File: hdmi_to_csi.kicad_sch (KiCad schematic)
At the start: 45 parts, among them P1 22P_FPC, U7 TC358743XBG_EL_NOK, U8 TLV62568DBVR, U9 TLV62568DBVR, X2 27MHz

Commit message: Preliminary Revision of PS176 DP->HDMI Subsystem
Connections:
- net CSI_2N: now also U7.B7 (CSID2N)
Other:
- note removed: "Solder this by hand to save money!!"

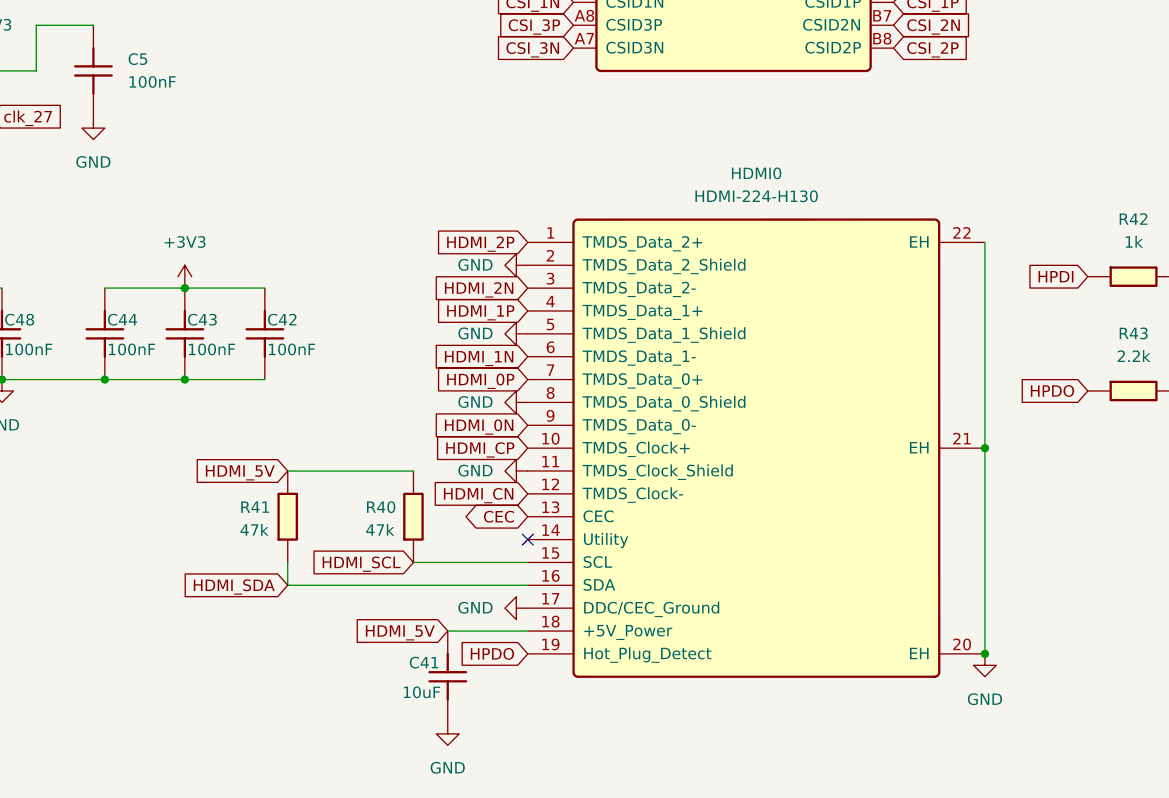
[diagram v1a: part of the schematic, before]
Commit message: Preliminary design of power monitor for PSU rails and USB-C VBUS
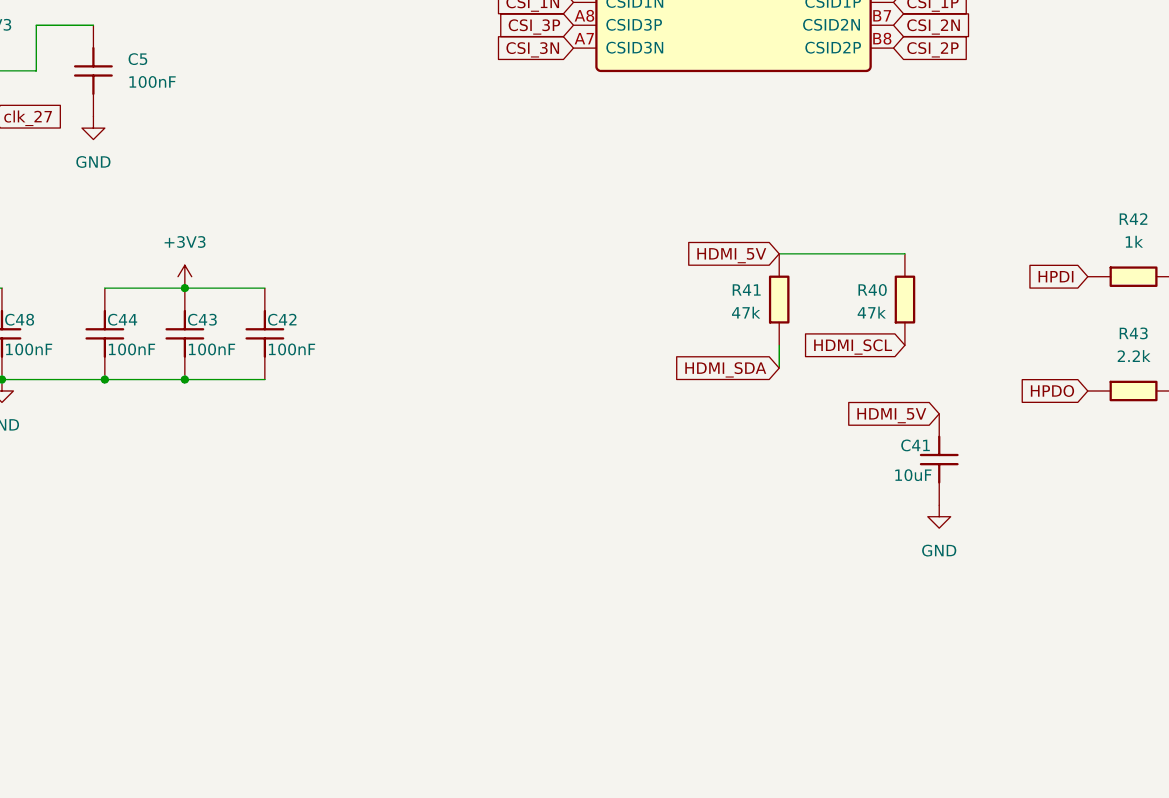
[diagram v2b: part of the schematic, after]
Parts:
- removed HDMI0: HDMI-224-H130, JLCImport:HDMI-224-H130, symbol JLCImport:HDMI-224-H130
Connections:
- no-connect marks 7 -> 6
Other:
- moved on the sheet: C41, R40, R41

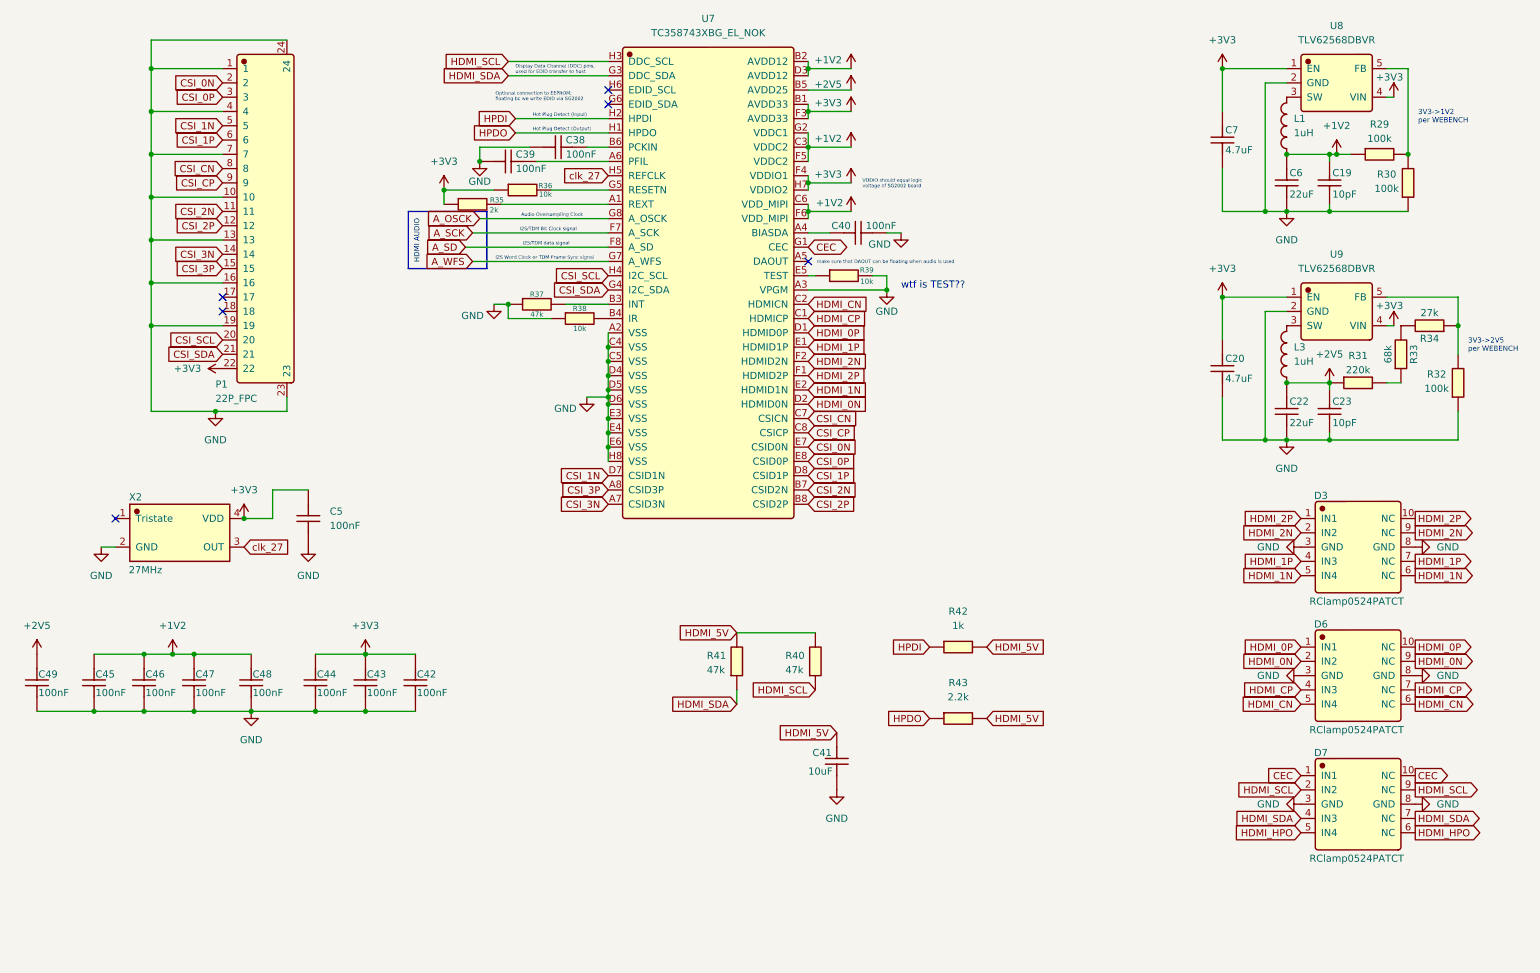
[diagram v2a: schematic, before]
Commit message: Preliminary design of power monitor for PS176, TC358743, LicheeRV nano, and touch display
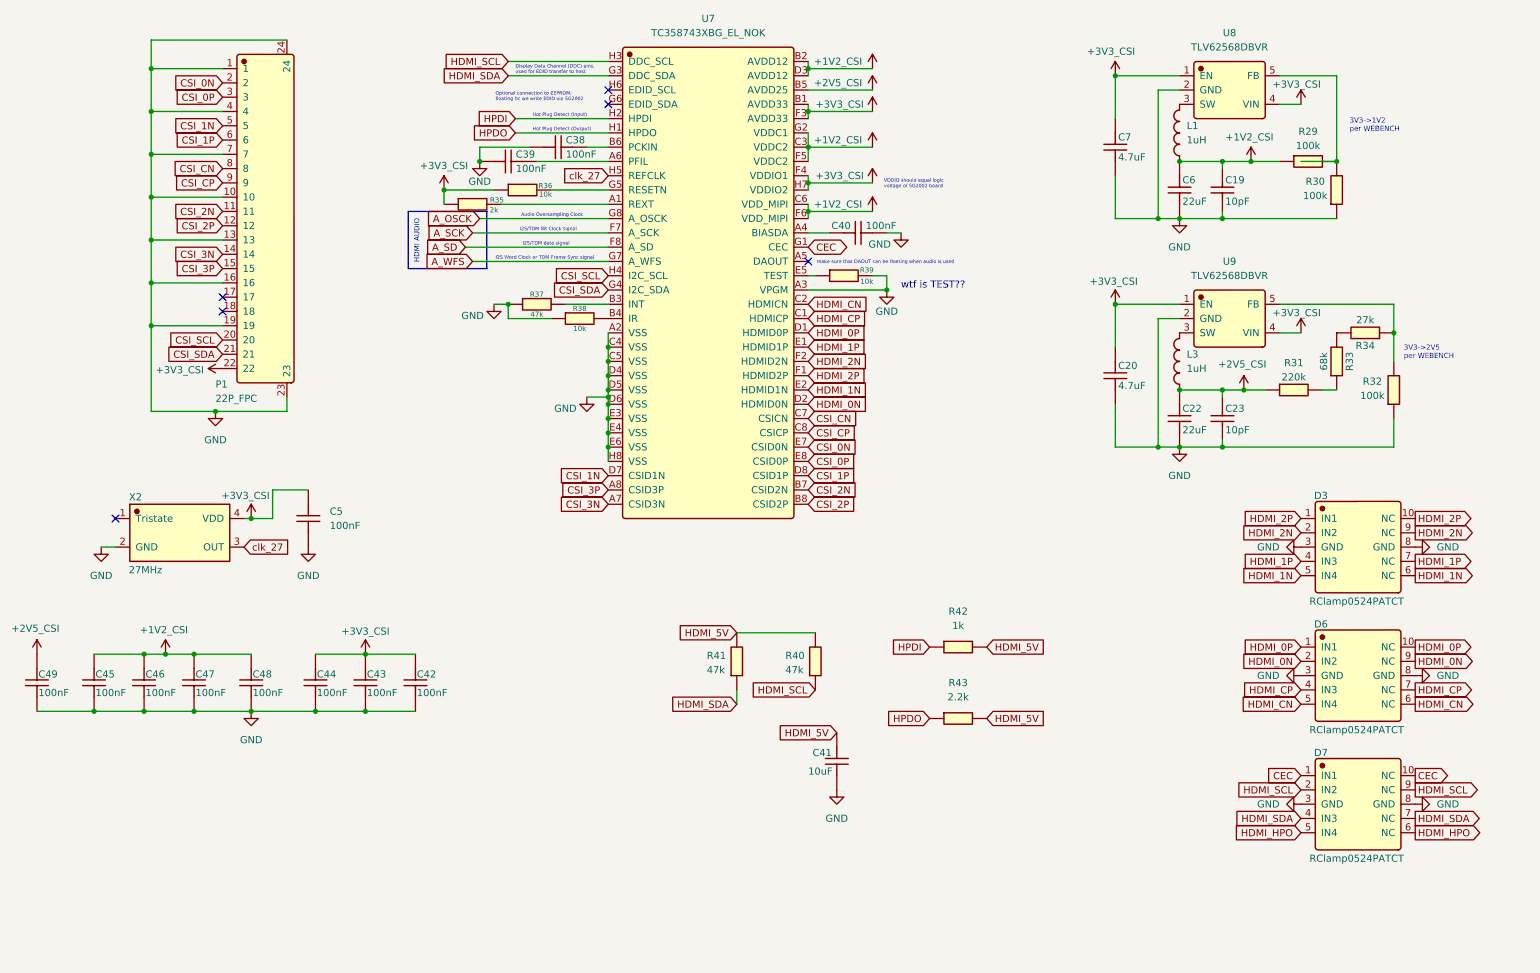
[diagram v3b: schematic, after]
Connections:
- net +1V2 renamed +1V2_CSI
- net +2V5 renamed +2V5_CSI
- net +3V3 renamed +3V3_CSI
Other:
- moved on the sheet: C19, C20, C22, C23, C6, C7, L1, L3, R29, R30, R31, R32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
